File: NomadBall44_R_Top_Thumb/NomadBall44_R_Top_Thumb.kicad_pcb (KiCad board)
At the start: 2 copper layers, 147.4 x 96.5 mm, 56 parts, among them SW1 SW_Push, SW10 SW_Push, SW11 SW_Push, SW12 SW_Push, SW13 SW_Push, SW14 SW_Push, SW15 SW_Push, SW16 SW_Push, SW17 SW_Push, SW18 SW_Push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

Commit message: ダイオードの削除 & キーホールとネジ用ホールを設定
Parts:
- removed D1, D10, D11, D12, D13, D14, D15, D16, D17, D18, D19, D2, D20, D21, D22, D3, D4, D5, D6, D7, D8, D9: D, NomadBall44:Diode_SMD
- REF** (x8): value MountingHole_4.3mm_M4 -> Val**; footprint MountingHole:MountingHole_4.3mm_M4 -> NomadBall44:m2_Screw_Hole
- SW19, SW20: footprint NomadBall44:Kailh_Choc_V1_Hotswap_thin_via -> NomadBall44:SW_Hole_1u

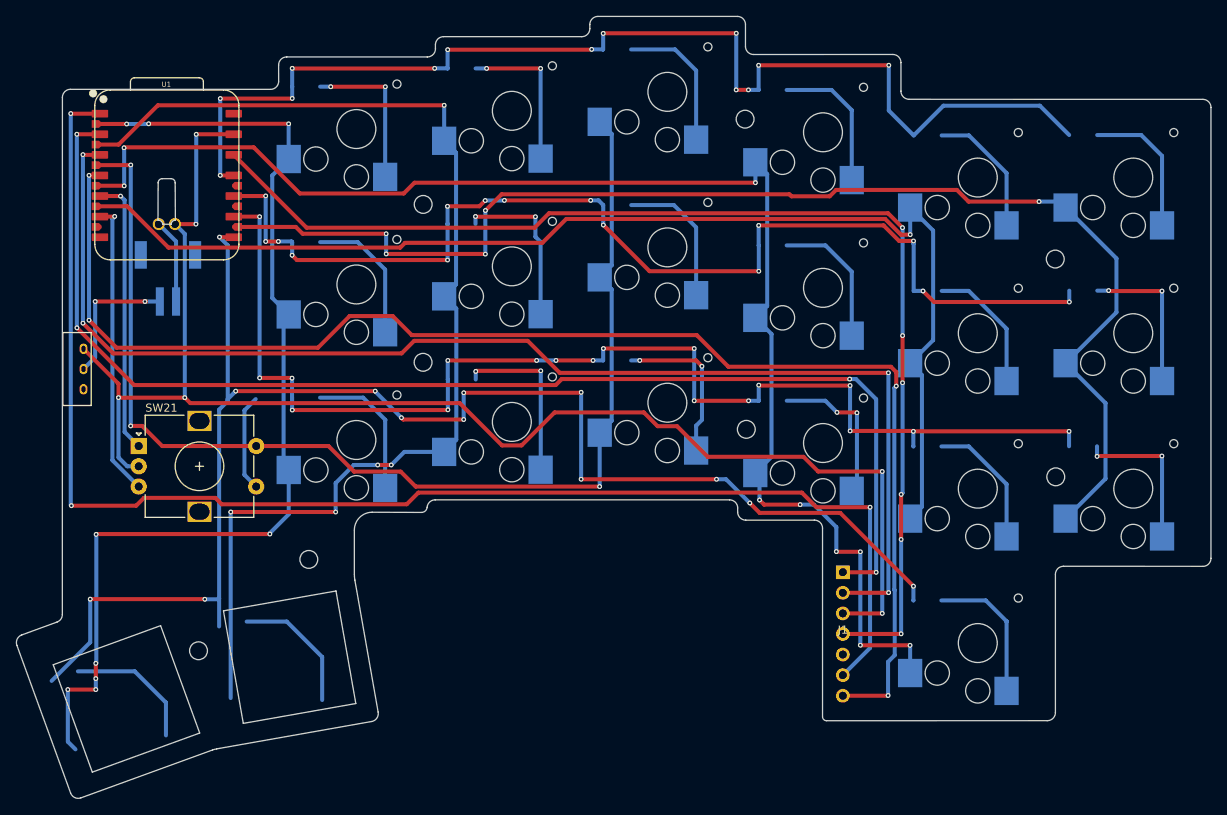
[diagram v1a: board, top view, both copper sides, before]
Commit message: 親指用の外形線を作成
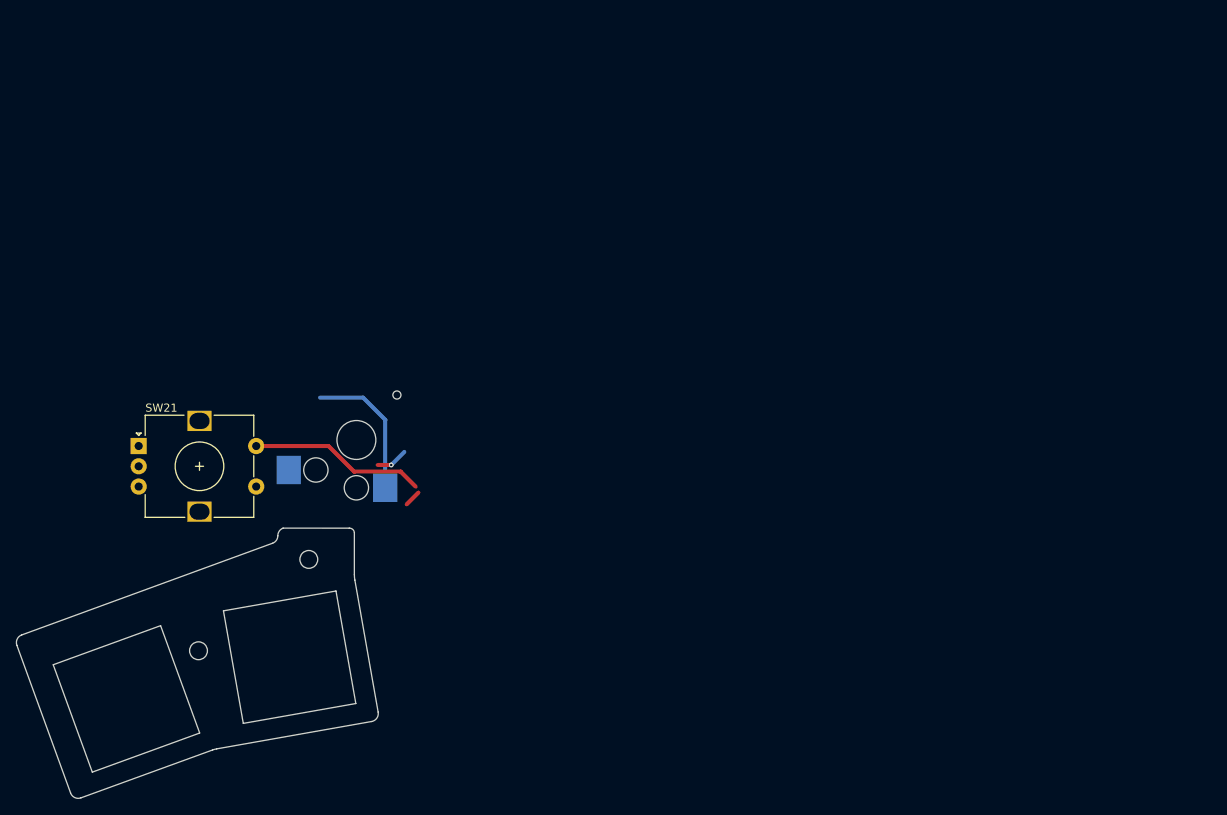
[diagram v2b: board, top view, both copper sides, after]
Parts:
- removed BT1: Battery_Cell, NomadBall44:JST_S2B-PH-SM4-TB
- removed J1: ~, NomadBall44:pmw3610_connector
- removed the REF** at (163.4, 91.7)
- removed the REF** at (201.5, 97.5)
- removed the REF** at (123.5, 83.4)
- removed the REF** at (163.2, 53.4)
- removed the REF** at (201.5, 70.7)
- removed the REF** at (123.5, 63.9)
- removed SW1, SW10, SW11, SW12, SW14, SW15, SW16, SW17, SW18, SW2, SW22, SW3, SW4, SW5, SW6, SW7, SW8, SW9: SW_Push, NomadBall44:Choc_v2_Hotswap_1u
- removed SW23: SW_SPDT, NomadBall44:TGSW_MSK-12D19
- removed U1: XIAO-nRF52840-Plus-SMD, NomadBall44:XIAO-nRF52840-Plus
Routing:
- net Row3: track 186.4 -> 0.00 mm, vias 13 -> 0
- net GND: track 182.4 -> 0.00 mm, vias 6 -> 0
- net Col3: track 174.5 -> 0.00 mm, vias 9 -> 0
- net SDIO: track 174.7 -> 2.03 mm, vias 3 -> 0
- net MOTION: track 170.7 -> 0.00 mm, vias 4 -> 0
- net Col5: track 160.3 -> 0.00 mm, vias 5 -> 0
- net CS: track 158.9 -> 0.00 mm, vias 4 -> 0
- net SCLK: track 155.1 -> 0.00 mm, vias 4 -> 0
- net Row2: track 152.2 -> 0.00 mm, vias 18 -> 0
- net Col4: track 150.0 -> 0.00 mm, vias 1 -> 0
- net 3.3V: track 145.1 -> 0.00 mm, vias 6 -> 0
- net Row0: track 143.9 -> 0.00 mm, vias 13 -> 0
- net Col1: track 144.5 -> 3.95 mm, vias 5 -> 1
- net Row1: track 137.2 -> 0.00 mm, vias 15 -> 0
- net Col0: track 130.0 -> 0.90 mm, vias 9 -> 0
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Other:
- board size 147.4 x 96.5 mm -> 44.6 x 33.3 mm

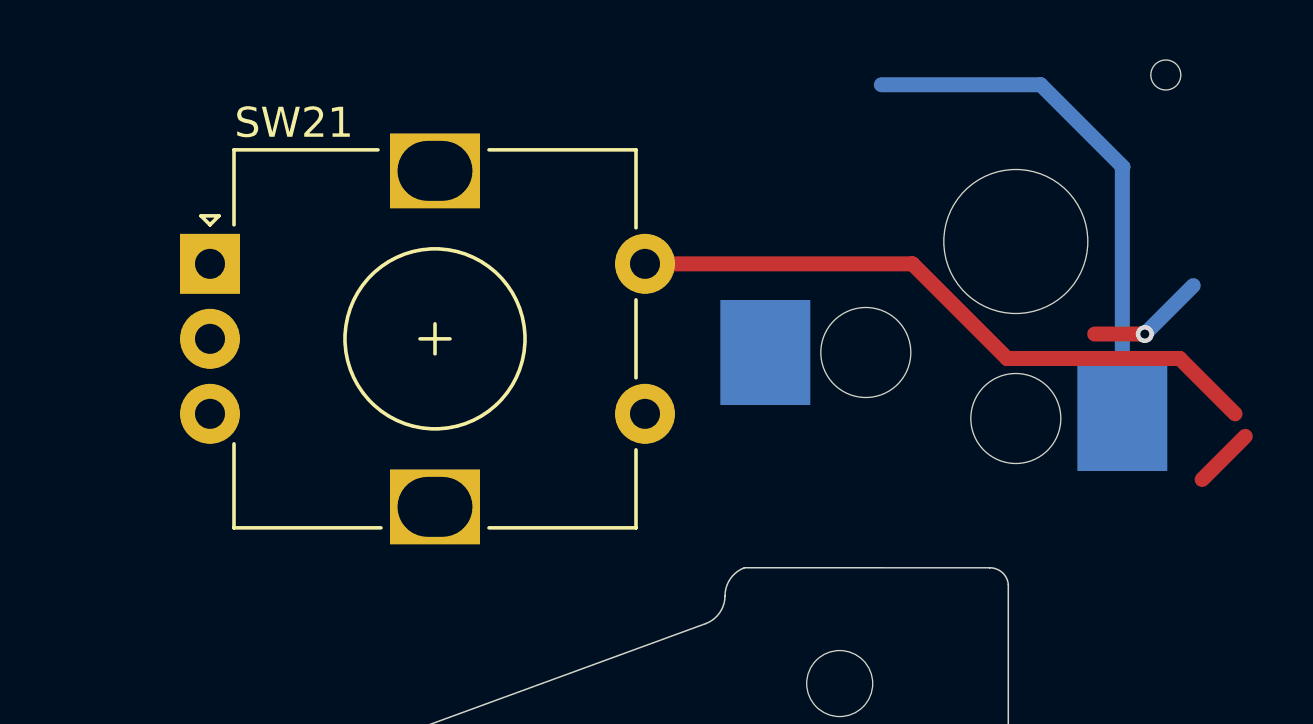
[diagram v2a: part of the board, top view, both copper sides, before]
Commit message: トッププレート（親指）のガーバファイルを生成
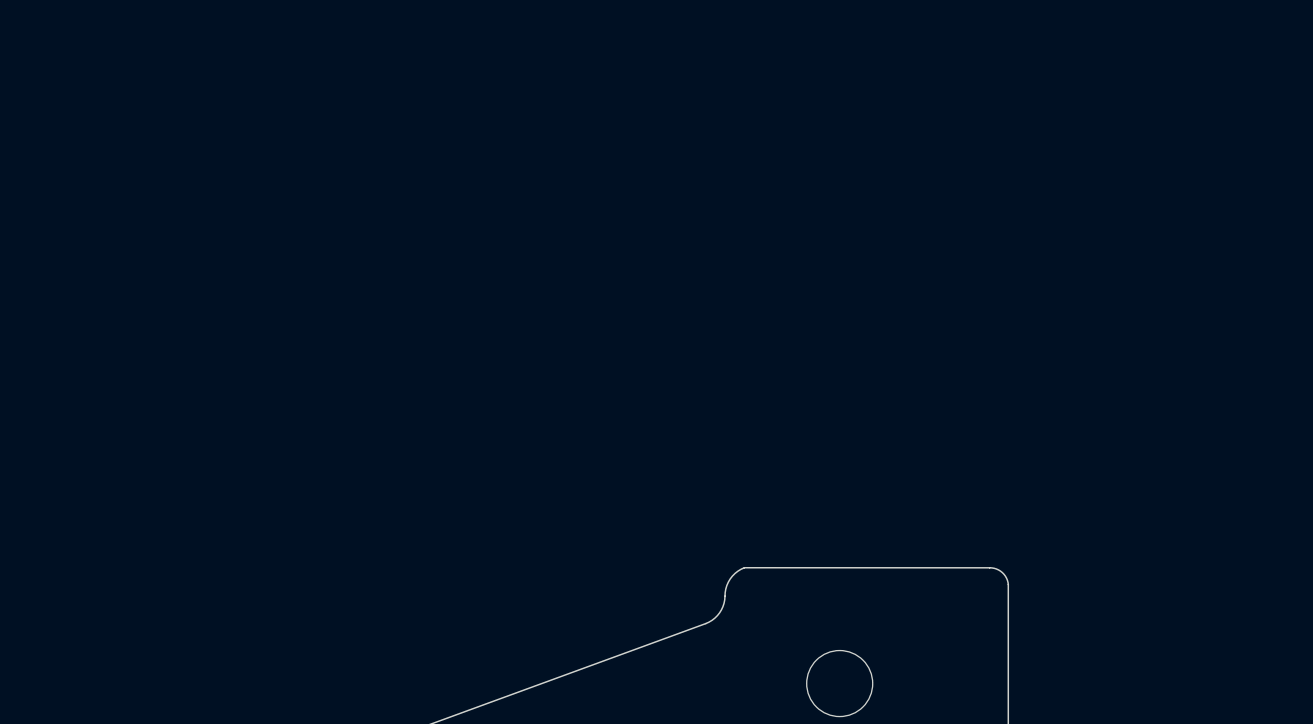
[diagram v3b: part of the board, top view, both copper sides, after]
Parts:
- removed SW13: SW_Push, NomadBall44:Choc_v2_Hotswap_1u
- removed SW21: RotaryEncoder_Switch, Rotary_Encoder:RotaryEncoder_Alps_EC12E-Switch_Vertical_H20mm
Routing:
- net Col2: track 21.7 -> 0.00 mm
- net Net-(D13-A): track 17.6 -> 0.00 mm
- net Col1: track 3.95 -> 0.00 mm, vias 1 -> 0
- net SDIO: track 2.03 -> 0.00 mm
- net Col0: track 0.90 -> 0.00 mm
